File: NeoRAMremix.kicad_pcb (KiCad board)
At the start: 2 copper layers, 58.2 x 84.1 mm, 28 parts, among them P1 C64-Exp-Port, Q1 2N3904, SW1 Reset, U1 HM628512BFP-5, U2 HM628512BFP-5, U3 HM628512BFP-5, U4 HM628512BFP-5

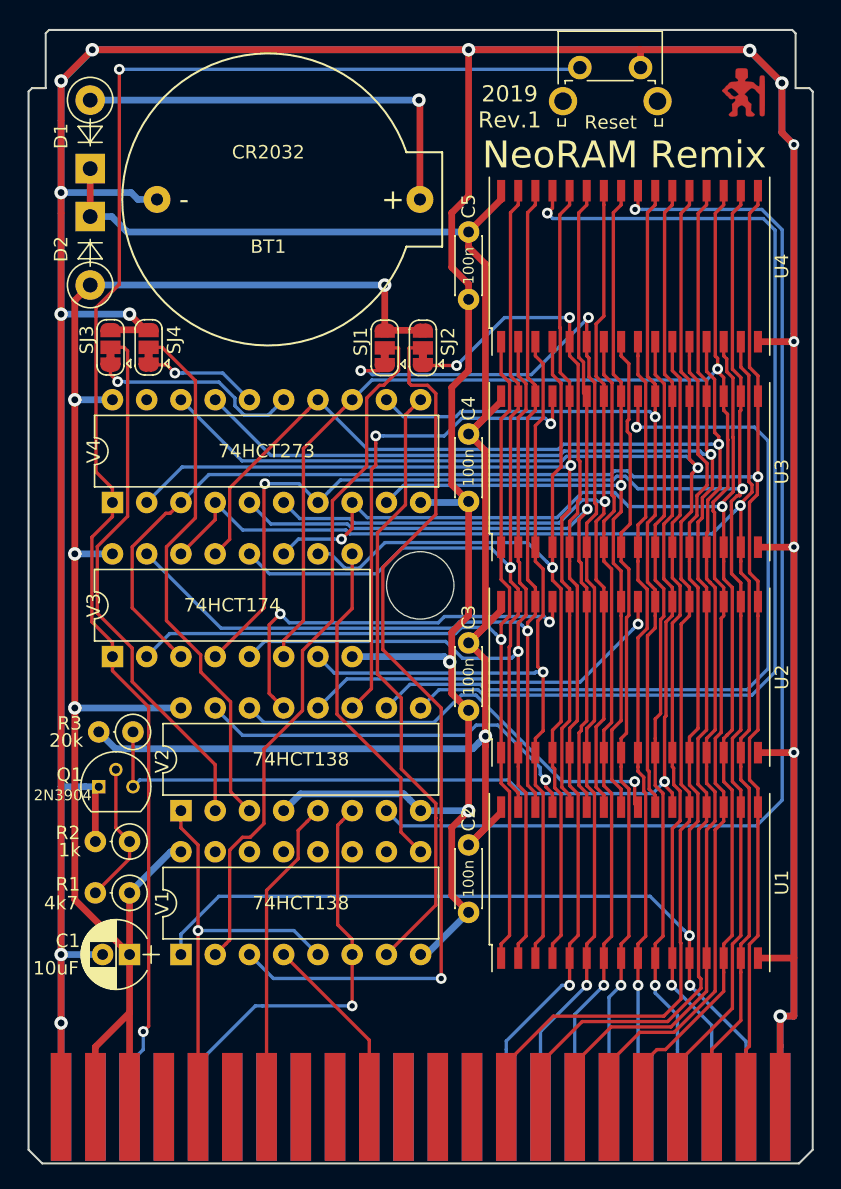
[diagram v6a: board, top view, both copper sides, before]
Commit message: Fixing RAM footprint.
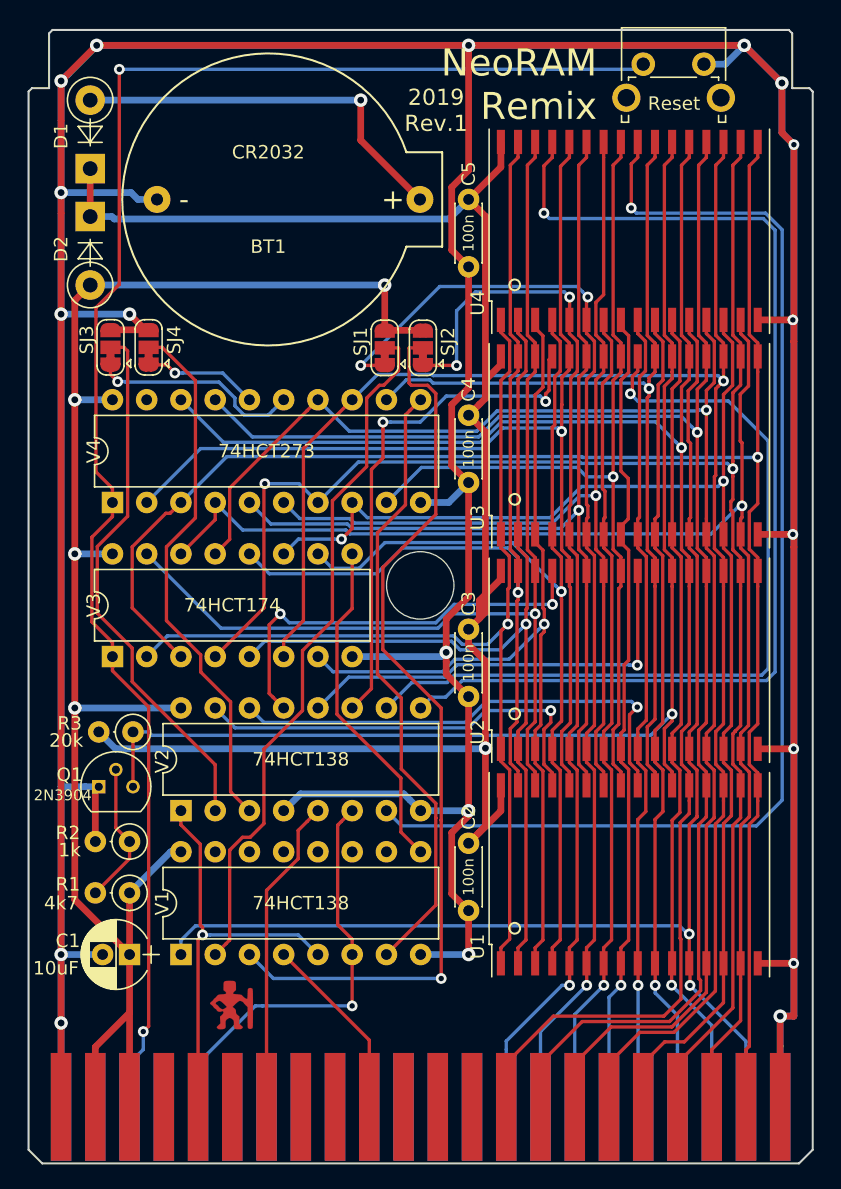
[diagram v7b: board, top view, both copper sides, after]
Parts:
- SJ1, SJ2, SJ3, SJ4: value (none) -> SolderJumper_3_Bridged12
- U1, U2, U3, U4: footprint Housings_SSOP:TSOP-II-32_21.0x10.2mm_Pitch1.27mm -> NeoRAMremix:SO32_FP32D_20.45x11.3mm_Pitch1.27mm
- moved G*** 77.6 mm to (99.1, 123.1)
- moved SW1 4.71 mm to (129.5, 53.3)
- moved U4 2.62 mm to (128.5, 65.7)
- moved C5 2.41 mm to (116.6, 63.4)
- moved U3 1.95 mm to (128.5, 81.6)
- moved C4 1.40 mm to (116.6, 79.4)
- moved U2 1.28 mm to (128.5, 97.5)
- moved C3 1.02 mm to (116.6, 95.2)
- moved U1 0.61 mm to (128.5, 113.4)
- moved C2 0.13 mm to (116.6, 111.1)
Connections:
- P1 pad 11: Net-(P1-Pad11) -> (no net)
- P1 pad 12: Net-(P1-Pad12) -> (no net)
- P1 pad 13: Net-(P1-Pad13) -> (no net)
- P1 pad 4: Net-(P1-Pad4) -> (no net)
- P1 pad 6: Net-(P1-Pad6) -> (no net)
- P1 pad 8: Net-(P1-Pad8) -> (no net)
- P1 pad 9: Net-(P1-Pad9) -> (no net)
- P1 pad B: Net-(P1-PadB) -> (no net)
- P1 pad D: Net-(P1-PadD) -> (no net)
- P1 pad F: /A15 -> (no net)
- P1 pad H: /A14 -> (no net)
- P1 pad J: /A13 -> (no net)
- P1 pad K: /A12 -> (no net)
- P1 pad L: /A11 -> (no net)
- P1 pad M: /A10 -> (no net)
- P1 pad N: /A9 -> (no net)
- P1 pad P: /A8 -> (no net)
- V1 pad 10: Net-(V1-Pad10) -> (no net)
- V1 pad 11: Net-(V1-Pad11) -> (no net)
- V1 pad 12: Net-(V1-Pad12) -> (no net)
- V1 pad 13: Net-(V1-Pad13) -> (no net)
- V1 pad 14: Net-(V1-Pad14) -> (no net)
- V1 pad 15: Net-(V1-Pad15) -> (no net)
- V4 pad 19: Net-(V4-Pad19) -> (no net)
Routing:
- net GND: track 555.7 -> 561.8 mm, vias 17 -> 19
- net Net-(P1-PadC): track 115.4 -> 120.2 mm
- net /RA15: track 68.6 -> 73.3 mm
- net +BATT: track 126.0 -> 130.7 mm
- net /A7: track 74.8 -> 79.5 mm
- net Net-(U4-Pad24): track 85.9 -> 89.9 mm
- net Net-(U2-Pad24): track 28.2 -> 32.0 mm
- net /D5: track 124.1 -> 127.8 mm
- net Net-(U4-Pad29): track 79.7 -> 83.4 mm
- net /D3: track 128.9 -> 132.3 mm
- net /RA12: track 66.7 -> 70.1 mm
- net /RA14: track 64.7 -> 68.0 mm
- net /RA16: track 68.3 -> 71.3 mm
- net /RA18: track 74.8 -> 77.6 mm
- net /RA13: track 79.9 -> 82.5 mm
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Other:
- outline, holes or cut-outs redrawn

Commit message: Preparing for rev.1
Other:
- board text added: "NeoRAM Remix Rev.1 Original design (2007): http://www.x1541.de/ Remix (2019): https://www.hackup.net/"
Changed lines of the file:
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@@
   (general
     (thickness 1.6)
-    (drawings 20)
+    (drawings 21)
     (tracks 1245)
     (zones 0)
@@
   (title_block
     (title "NeoRAM Remix")
+    (date 2019-01-17)
     (rev 1)
     (company hackup.net)
@@
     (34 B.Paste user)
     (35 F.Paste user)
-    (36 B.SilkS user)
+    (36 B.SilkS user hide)
     (37 F.SilkS user)
     (38 B.Mask user)
@@
     )
   )
+  (gr_text "NeoRAM Remix Rev.1\nOriginal design (2007): http://www.x1541.de/\nRemix (2019): https://www.hackup.net/" (at 140.335 73.025) (layer B.SilkS)
+    (effects (font (size 1.5 1.5) (thickness 0.3)) (justify left mirror))
+  )
   (gr_line (start 142.113 55.372) (end 141.859 55.118) (layer Edge.Cuts) (width 0.15))
